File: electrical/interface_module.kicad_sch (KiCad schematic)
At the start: 22 parts, among them J1 Screw_Terminal_01x01, K2 Starter RELAY, SW3 NEUTRAL DETECT, SW4 KILL SWITCH, SW5 STARTER SWITCH

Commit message: electrical module draft
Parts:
- removed C6, C7: 15n, symbol Device:C
- removed D1 (x2): BZX55C 4.7V, Diode_THT:D_DO-35_SOD27_P7.62mm_Horizontal, symbol Diode:BZX84Cxx
- removed D10: P6KE20CA, Diode_THT:D_DO-15_P12.70mm_Horizontal, symbol Diode:SD15_SOD323
- removed D13, D7, D9: 1N4148, Diode_THT:D_DO-35_SOD27_P7.62mm_Horizontal, symbol Diode:1N4148
- removed F5: ~, symbol Device:Fuse
- removed J1: Screw_Terminal_01x01, symbol Connector:Screw_Terminal_01x01
- removed K2: Starter RELAY, Relay_THT:Relay_SPST_StandexMeder_SIL_Form1A, symbol Relay:SILxx-1Axx-71x
- removed R10, R12: 22k, symbol Device:R
- removed R11, R13: 10k, symbol Device:R
- removed SW4: KILL SWITCH, symbol Switch:SW_SPST
- added C4: 15n, symbol Device:C
- added D4: 1N4148, Diode_THT:D_DO-35_SOD27_P7.62mm_Horizontal, symbol Diode:1N4148
- SW5: value STARTER SWITCH -> OLI PRESSURE SWITCH
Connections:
- net GND: now also C4.2
- net GND when NO oli pressure: now reaches J1.1 (Pin_1), SW5.2 (B)
- net GND when NO oli pressure: now also D4.1 (K)
- net GND when no gear engaged: now reaches D4.1 (K), J1.1 (Pin_1), SW3.2 (B)
- new net OLI PRESSURE: C4.1, D4.2 (A)
- no-connect marks 2 -> 0
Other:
- note removed: "Those two lines are interchangeable"
- moved on the sheet: C4, D4, J1, SW5

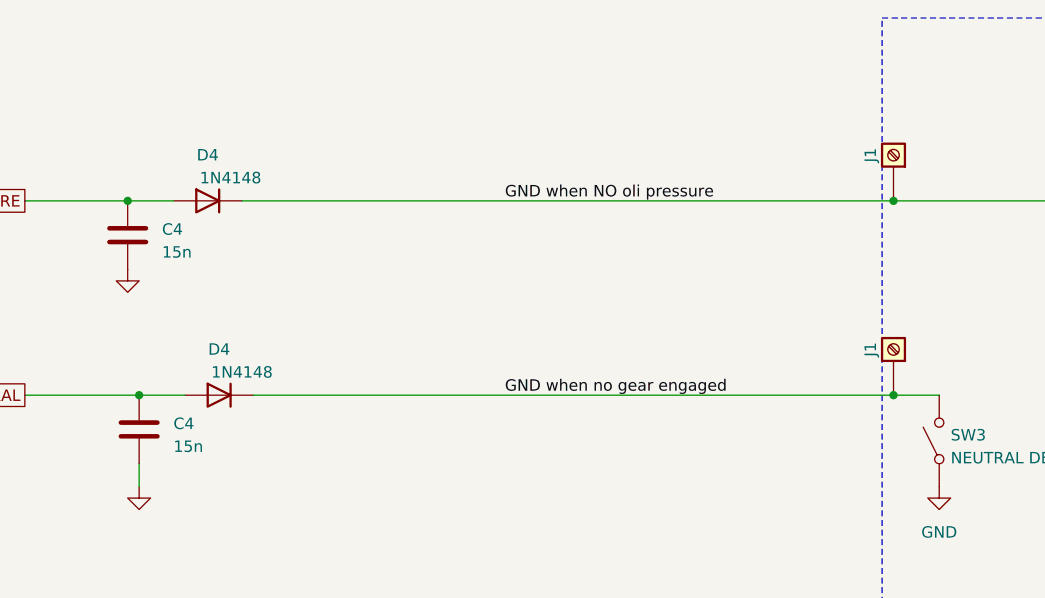
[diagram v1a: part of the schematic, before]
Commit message: Aktualizacja KiCad i schematu - LED do debugowania
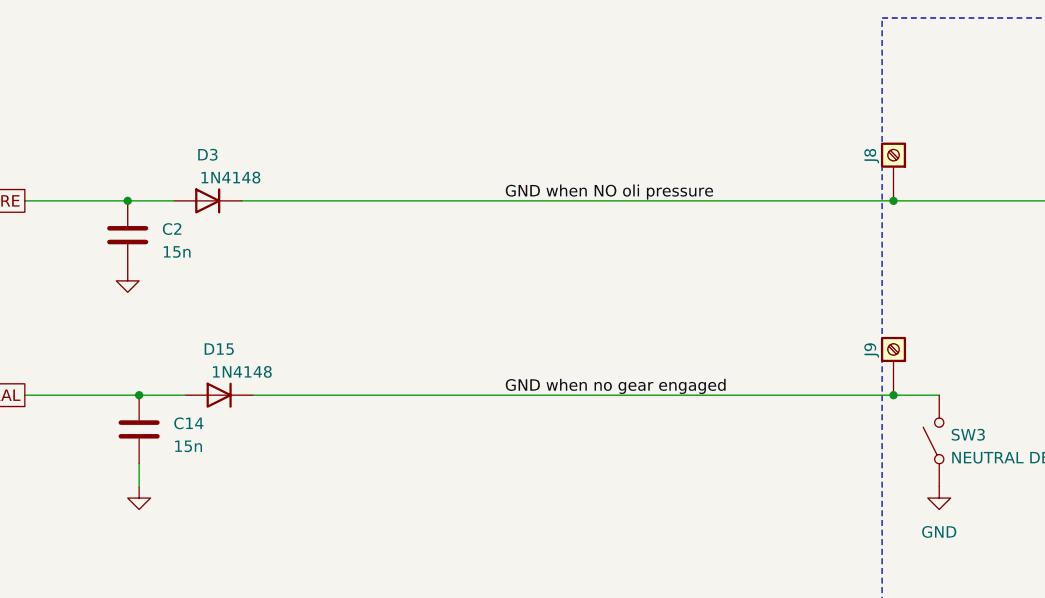
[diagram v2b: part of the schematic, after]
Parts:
- renumbered C4 to C14, C4 to C2, D4 to D15, D4 to D3, J1 to J8, J1 to J9
